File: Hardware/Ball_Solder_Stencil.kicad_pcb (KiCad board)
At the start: 4 copper layers, 99.8 x 102.2 mm, 88 parts, among them Q1 SI2333DS, U1 STM32WB35, U2 L3GD20, U2 LD1117-3.3-4Tab, U3 MCP73831-2-OT, U3 TL074, U4 LD3985M28R_SOT23, U4 TL072, Y1 32MHz, Y2 32.768MHz

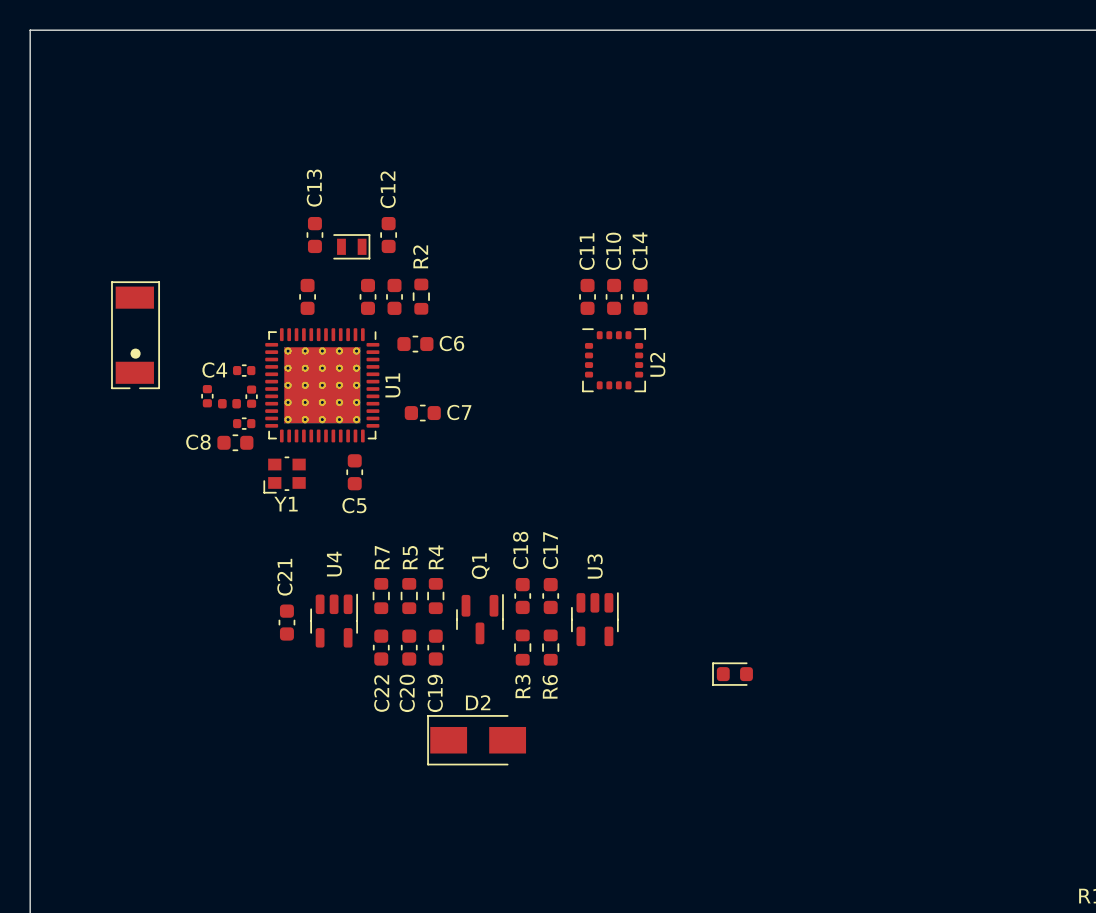
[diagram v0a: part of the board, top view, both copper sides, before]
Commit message: More PCB clean-up
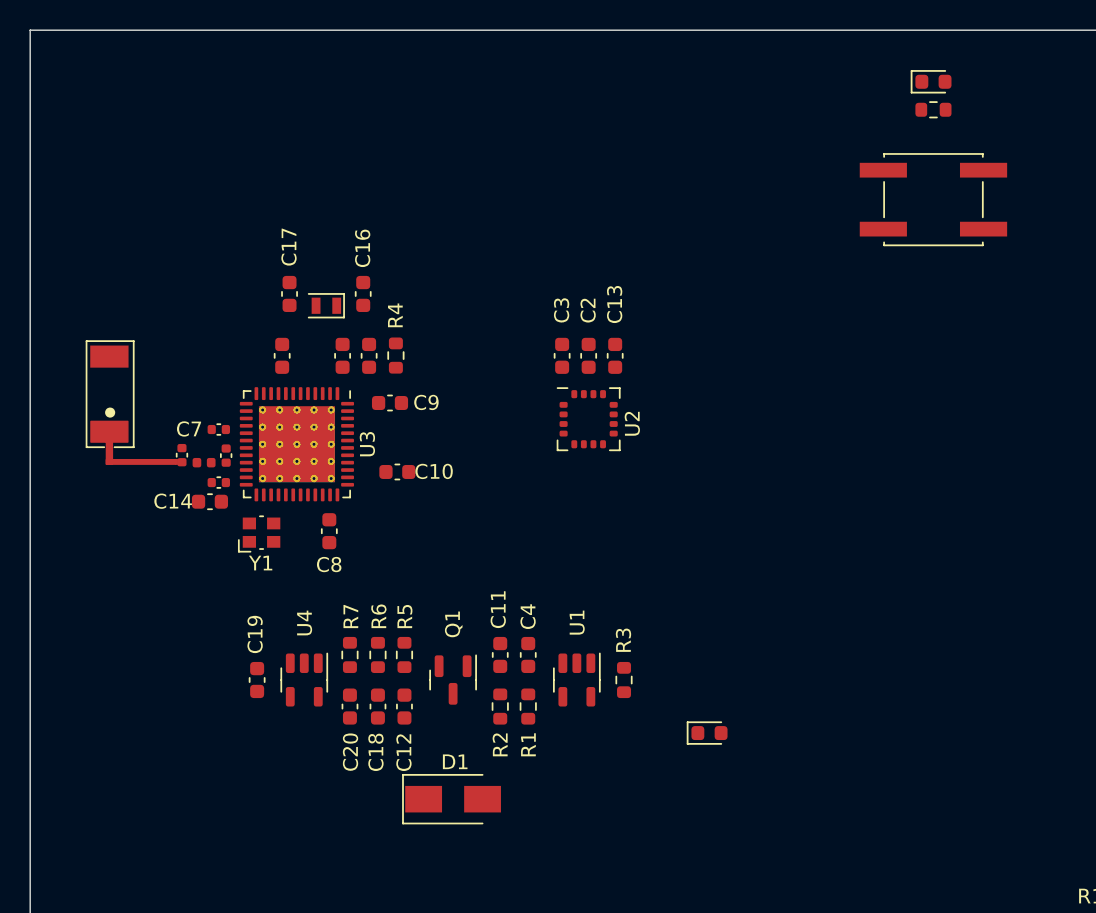
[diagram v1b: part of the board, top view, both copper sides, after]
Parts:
- added CONNECT1: SW_Push, Button_Switch_SMD:SW_SPST_EVQQ2, F.Cu at (126.3, 67.1)
- added D1: PMEG3010ER, Diode_SMD:D_SMA, F.Cu at (93.7, 107.8)
- added R1: 1k, Resistor_SMD:R_0603_1608Metric, F.Cu at (98.8, 101.5)
- added R8: 1k, Resistor_SMD:R_0603_1608Metric, F.Cu at (126.3, 61.0)
- C11: value 10uF -> 4.7uF
- C12: value 16pF -> 1uF
- C13: value 16pF -> 10nF
- C14: value 10nF -> 100nF
- C15: value 0.8pF -> 100pF
- C16: value 0.3pF -> 16pF; footprint Capacitor_SMD:C_0402_1005Metric -> Capacitor_SMD:C_0603_1608Metric
- C17: value 4.7uF -> 16pF
- C18: value 4.7uF -> 1uF
- C19: value 1uF -> 10nF
- C2: value 4.7uF -> 100nF
- C21: value 10nF -> 0.8pF; footprint Capacitor_SMD:C_0603_1608Metric -> Capacitor_SMD:C_0402_1005Metric
- C22: value 1uF -> 0.3pF; footprint Capacitor_SMD:C_0603_1608Metric -> Capacitor_SMD:C_0402_1005Metric
- C3: value 100nF -> 10uF
- C4: value 100nF -> 4.7uF; footprint Capacitor_SMD:C_0402_1005Metric -> Capacitor_SMD:C_0603_1608Metric
- C5: value 100nF -> 4.7uF
- C7: footprint Capacitor_SMD:C_0603_1608Metric -> Capacitor_SMD:C_0402_1005Metric
- C9: value 100pF -> 100nF; footprint Capacitor_SMD:C_0402_1005Metric -> Capacitor_SMD:C_0603_1608Metric
- D2: value PMEG3010ER -> LED_CHG; footprint Diode_SMD:D_SMA -> LED_SMD:LED_0603_1608Metric
- D3: value LED_CHG -> LED_CONNECT
- R3: value 1k -> 10k
- R4: value 27k -> 100k
- R5: value 13k -> 27k
- R6: value 10k -> 13k
- U1: value STM32WB35 -> MCP73831-2-OT; footprint Package_DFN_QFN:QFN-48-1EP_7x7mm_P0.5mm_EP5.15x5.15mm_ThermalVias -> Package_TO_SOT_SMD:SOT-23-5
- U3: value MCP73831-2-OT -> STM32WB35; footprint Package_TO_SOT_SMD:SOT-23-5 -> Package_DFN_QFN:QFN-48-1EP_7x7mm_P0.5mm_EP5.15x5.15mm_ThermalVias
- moved D3 42.4 mm to (126.3, 59.1)
- moved C14 32.4 mm to (77.2, 87.6), turned to 180 degrees
- moved C12 32.0 mm to (90.4, 101.5)
- moved R2 28.3 mm to (96.9, 101.5)
- moved C4 27.3 mm to (98.8, 98.0), turned to 90 degrees
- moved C17 27.1 mm to (82.6, 73.5), turned to -90 degrees
- moved U1 26.4 mm to (102.1, 99.7)
- moved C11 25.0 mm to (96.9, 98.0), turned to -90 degrees
- moved U3 23.5 mm to (83.1, 83.7)
- moved C13 22.0 mm to (104.7, 77.7), turned to 90 degrees
- moved C10 18.9 mm to (89.9, 85.6), turned to 0 degrees
- moved C22 18.8 mm to (75.3, 84.4)
- moved R4 16.5 mm to (89.8, 77.7)
- moved D2 15.7 mm to (111.1, 103.3)
- moved C7 13.9 mm to (77.8, 82.7), turned to 180 degrees
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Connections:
- AE1 pad 1: (no net) -> Net-(AE1-Pad1)
- AE1 pad 2: (no net) -> unconnected-(AE1-Pad2)
- C12 pad 1: GND -> VCC
- C12 pad 2: (no net) -> GND
- C13 pad 1: GND -> (no net)
- C13 pad 2: (no net) -> GND
- C15 pad 1: /RF_Output -> (no net)
- C16 pad 1: Net-(AE1-Pad1) -> GND
- C16 pad 2: GND -> (no net)
- C17 pad 1: (no net) -> GND
- C17 pad 2: GND -> Net-(C17-Pad2)
- C18 pad 1: (no net) -> VCC
- C19 pad 1: VCC -> (no net)
- C20 pad 1: VCC -> (no net)
- C21 pad 1: (no net) -> /RF_Output
- C22 pad 1: (no net) -> Net-(AE1-Pad1)
- D2 pad 1: VCC -> (no net)
- D3 pad 1: (no net) -> Net-(D3-Pad1)
- D3 pad 2: (no net) -> /LED_BLUE_OUT
- R2 pad 2: /BOOT0 -> (no net)
- R3 pad 1: (no net) -> GND
- R4 pad 1: VCC -> GND
- R4 pad 2: (no net) -> /BOOT0
- R5 pad 1: (no net) -> VCC
- R6 pad 1: GND -> (no net)
- U1 pad 2: (no net) -> GND
- U1 pad 4: /BOOT0 -> (no net)
- U3 pad 2: GND -> (no net)
- U3 pad 3: (no net) -> Net-(C17-Pad2)
- U3 pad 4: (no net) -> /BOOT0
- Y1 pad 1: Net-(U1-Pad24) -> (no net)
- Y1 pad 3: Net-(U1-Pad25) -> (no net)
- Y2 pad 2: (no net) -> Net-(C17-Pad2)

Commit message: Preparation of Gerbers for manufacturing
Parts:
- removed the AE1 at (74.9, 84.9)
- removed the AE1 at (128.4, 147.8)
- removed the C1 at (141.3, 140.6)
- removed the C1 at (82.1, 77.7)
- removed the C10 at (89.9, 85.6)
- removed the C10 at (155.2, 90.7)
- removed the C11 at (96.9, 98.0)
- removed the C11 at (155.2, 60.5)
- removed the C12 at (131.8, 147.4)
- removed the C12 at (90.4, 101.5)
- removed the C13 at (104.7, 77.7)
- removed the C13 at (128.8, 147.3)
- removed the C14 at (157.3, 109.8)
- removed the C14 at (77.2, 87.6)
- removed the C15 at (77.8, 86.3)
- removed the C15 at (140.4, 128.0)
- removed the C16 at (87.6, 73.5)
- removed the C16 at (152.6, 128.0)
- removed the C17 at (82.6, 73.5)
- removed the C17 at (140.4, 129.7)
- removed the C18 at (88.6, 101.5)
- removed the C18 at (152.6, 126.3)
- removed the C19 at (152.6, 117.8)
- removed the C19 at (80.4, 99.7)
- removed the C2 at (102.9, 77.7)
- removed the C2 at (139.5, 140.6)
- removed the C20 at (86.7, 101.5)
- removed the C20 at (152.6, 124.6)
- removed the C21 at (78.3, 84.5)
- removed the C21 at (140.4, 119.5)
- removed the C22 at (140.4, 124.6)
- removed the C22 at (75.3, 84.4)
- removed the C3 at (101.1, 77.7)
- removed the C3 at (131.3, 145.6)
- removed the C4 at (138.8, 152.5)
- removed the C4 at (98.8, 98.0)
- removed the C5 at (142.9, 143.8)
- removed the C5 at (88.0, 77.7)
- removed the C6 at (142.9, 147.8)
- removed the C6 at (86.2, 77.7)
- removed the C7 at (135.9, 140.6)
- removed the C7 at (77.8, 82.7)
- removed the C8 at (130.7, 150.5)
- removed the C8 at (85.3, 89.6)
- removed the C9 at (89.4, 80.9)
- removed the C9 at (131.3, 149.2)
- removed the D1 at (159.7, 90.7)
- removed the D1 at (93.7, 107.8)
- removed the D2 at (111.1, 103.3)
- removed the D2 at (159.7, 60.5)
- removed the D3 at (126.3, 59.1)
- removed the L1 at (76.8, 85.0)
- removed the L1 at (130.3, 147.8)
- removed the Q1 at (93.7, 99.7)
- removed the R1 at (98.8, 101.5)
- removed the R1 at (137.7, 140.6)
- removed the R10 at (140.4, 121.2)
- removed the R11 at (140.4, 122.9)
- removed the R12 at (140.4, 116.1)
- removed the R13 at (140.4, 117.8)
- removed the R14 at (152.6, 116.1)
- removed the R15 at (140.4, 126.3)
- removed the R16 at (140.4, 114.4)
- removed the R17 at (130.8, 143.2)
- removed the R2 at (140.4, 131.4)
- removed the R2 at (96.9, 101.5)
- removed the R3 at (105.3, 99.7)
- removed the R3 at (152.6, 129.7)
- removed the R4 at (152.6, 133.1)
- removed the R4 at (89.8, 77.7)
- removed the R5 at (152.6, 131.4)
- removed the R5 at (90.4, 98.0)
- removed the R6 at (88.6, 98.0)
- removed the R6 at (140.4, 133.1)
- removed the R7 at (86.7, 98.0)
- removed the R7 at (152.6, 122.9)
- removed the R8 at (126.3, 61.0)
- removed the R8 at (152.6, 119.5)
- removed the R9 at (152.6, 121.2)
- removed the U1 at (102.1, 99.7)
- removed the U1 at (136.6, 146.6)
- removed the U2 at (102.9, 82.0)
- removed the U2 at (157.3, 100.2)
- removed the U3 at (83.1, 83.7)
- removed the U3 at (146.5, 128.5)
- removed the U4 at (83.6, 99.7)
- removed the U4 at (146.5, 117.0)
- removed the Y1 at (134.2, 152.6)
- removed the Y1 at (80.7, 89.7)
- added AE1: Antenna_Shield, Custom_Footprints:NN01_102, F.Cu at (125.9, 132.9)
- added AE1: Antenna_Shield, Custom_Footprints:NN01_102, F.Cu at (214.0, 94.9)
- added C1: 4.7uF, Capacitor_SMD:C_0603_1608Metric, F.Cu at (138.7, 125.8)
- added C1: 4.7uF, Capacitor_SMD:C_0603_1608Metric, F.Cu at (58.4, 96.8)
- added C1: 100nF, Capacitor_SMD:C_0603_1608Metric, F.Cu at (221.2, 87.7)
- added C10: 22uF, Capacitor_SMD:CP_Elec_4x5.4, F.Cu at (148.9, 75.8)
- added C10: 100nF, Capacitor_SMD:C_0603_1608Metric, F.Cu at (229.0, 95.6)
- added C10: 18pF, Capacitor_SMD:C_0603_1608Metric, F.Cu at (52.5, 99.7)
- added C11: 18pF, Capacitor_SMD:C_0603_1608Metric, F.Cu at (52.5, 103.5)
- added C11: 4.7uF, Capacitor_SMD:C_0603_1608Metric, F.Cu at (236.0, 108.0)
- added C11: 22uF, Capacitor_SMD:CP_Elec_4x5.4, F.Cu at (148.9, 45.6)
- added C12: 0.8pF, Capacitor_SMD:C_0402_1005Metric, F.Cu at (129.2, 132.5)
- added C12: 2.2nF, Capacitor_SMD:C_0603_1608Metric, F.Cu at (68.4, 128.1)
- added C12: 1uF, Capacitor_SMD:C_0603_1608Metric, F.Cu at (229.5, 111.5)
- added C13: 0.3pF, Capacitor_SMD:C_0402_1005Metric, F.Cu at (126.2, 132.5)
- added C13: 10nF, Capacitor_SMD:C_0603_1608Metric, F.Cu at (243.8, 87.7)
- added C13: 1.5nF, Capacitor_SMD:C_0603_1608Metric, F.Cu at (68.4, 116.1)
- added C14: 47uF, Capacitor_SMD:CP_Elec_5x5.8, F.Cu at (151.0, 95.0)
- added C14: 2.2nF, Capacitor_SMD:C_0603_1608Metric, F.Cu at (55.6, 116.1)
- added C14: 100nF, Capacitor_SMD:C_0603_1608Metric, F.Cu at (216.3, 97.6)
- added C15: 100nF, Capacitor_SMD:C_0603_1608Metric, F.Cu at (134.1, 113.2)
- added C15: 100pF, Capacitor_SMD:C_0402_1005Metric, F.Cu at (216.9, 96.3)
- added C15: 1.5nF, Capacitor_SMD:C_0603_1608Metric, F.Cu at (55.6, 128.1)
- added C16: 16pF, Capacitor_SMD:C_0603_1608Metric, F.Cu at (226.7, 83.5)
- added C16: 18pF, Capacitor_SMD:C_0603_1608Metric, F.Cu at (55.6, 84.0)
- added C16: 100nF, Capacitor_SMD:C_0603_1608Metric, F.Cu at (146.3, 113.2)
- added C17: 22nF, Capacitor_SMD:C_0603_1608Metric, F.Cu at (134.1, 114.8)
- added C17: 16pF, Capacitor_SMD:C_0603_1608Metric, F.Cu at (221.7, 83.5)
- added C17: 10uF, Capacitor_SMD:C_0603_1608Metric, F.Cu at (55.6, 89.7)
- added C18: 1uF, Capacitor_SMD:C_0603_1608Metric, F.Cu at (227.7, 111.5)
- added C18: 33nF, Capacitor_SMD:C_0603_1608Metric, F.Cu at (146.3, 111.5)
- added C18: 18pF, Capacitor_SMD:C_0603_1608Metric, F.Cu at (68.4, 84.0)
- added C19: 10uF, Capacitor_SMD:C_0603_1608Metric, F.Cu at (68.4, 89.7)
- added C19: 22nF, Capacitor_SMD:C_0603_1608Metric, F.Cu at (146.3, 103.0)
- added C19: 10nF, Capacitor_SMD:C_0603_1608Metric, F.Cu at (219.5, 109.7)
- added C2: 100nF, Capacitor_SMD:C_0603_1608Metric, F.Cu at (136.9, 125.8)
- added C2: 100nF, Capacitor_SMD:C_0603_1608Metric, F.Cu at (62.6, 111.9)
- added C2: 100nF, Capacitor_SMD:C_0603_1608Metric, F.Cu at (242.0, 87.7)
- added C20: 1uF, Capacitor_SMD:C_0603_1608Metric, F.Cu at (225.8, 111.5)
- added C20: 10uF, Capacitor_SMD:C_0805_2012Metric, F.Cu at (51.7, 52.4)
- added C20: 33nF, Capacitor_SMD:C_0603_1608Metric, F.Cu at (146.3, 109.8)
- added C21: 22uF, Capacitor_SMD:CP_Elec_4x5.3, F.Cu at (80.8, 72.8)
- added C21: 22nF, Capacitor_SMD:C_0603_1608Metric, F.Cu at (134.1, 104.7)
- added C21: 0.8pF, Capacitor_SMD:C_0402_1005Metric, F.Cu at (217.4, 94.5)
- added C22: 33nF, Capacitor_SMD:C_0603_1608Metric, F.Cu at (134.1, 109.8)
- added C22: 0.3pF, Capacitor_SMD:C_0402_1005Metric, F.Cu at (214.4, 94.4)
- added C22: 47uF, Capacitor_SMD:CP_Elec_5x5.4, F.Cu at (59.9, 52.4)
- added C23: 100nF, Capacitor_SMD:C_0603_1608Metric, F.Cu at (37.6, 74.0)
- added C24: 22uF, Capacitor_SMD:CP_Elec_4x5.3, F.Cu at (42.9, 72.8)
- added C3: 100nF, Capacitor_SMD:C_0603_1608Metric, F.Cu at (69.3, 111.9)
- added C3: 100nF, Capacitor_SMD:C_0402_1005Metric, F.Cu at (128.7, 130.8)
- added C3: 10uF, Capacitor_SMD:C_0603_1608Metric, F.Cu at (240.2, 87.7)
- added C4: 4.7uF, Capacitor_SMD:C_0603_1608Metric, F.Cu at (237.9, 108.0)
- added C4: 100nF, Capacitor_SMD:C_0603_1608Metric, F.Cu at (136.2, 137.7)
- added C4: 100nF, Capacitor_SMD:C_0603_1608Metric, F.Cu at (74.4, 98.8)
- added C5: 100nF, Capacitor_SMD:C_0603_1608Metric, F.Cu at (140.4, 128.9)
- added C5: 100nF, Capacitor_SMD:C_0603_1608Metric, F.Cu at (61.6, 94.3)
- added C5: 4.7uF, Capacitor_SMD:C_0603_1608Metric, F.Cu at (227.1, 87.7)
- added C6: 100nF, Capacitor_SMD:C_0603_1608Metric, F.Cu at (225.3, 87.7)
- added C6: 100nF, Capacitor_SMD:C_0603_1608Metric, F.Cu at (140.3, 132.9)
- added C6: 1uF, Capacitor_SMD:C_0603_1608Metric, F.Cu at (56.4, 108.3)
- added C7: 100nF, Capacitor_SMD:C_0603_1608Metric, F.Cu at (133.3, 125.8)
- added C7: 100nF, Capacitor_SMD:C_0402_1005Metric, F.Cu at (216.9, 92.7)
- added C7: 100nF, Capacitor_SMD:C_0603_1608Metric, F.Cu at (56.4, 106.6)
- added C8: 100nF, Capacitor_SMD:C_0603_1608Metric, F.Cu at (128.1, 135.7)
- added C8: 100nF, Capacitor_SMD:C_0603_1608Metric, F.Cu at (224.4, 99.6)
- added C8: 2.2uF, Capacitor_SMD:C_0603_1608Metric, F.Cu at (67.6, 111.9)
- added C9: 100pF, Capacitor_SMD:C_0402_1005Metric, F.Cu at (128.7, 134.3)
- added C9: 100nF, Capacitor_SMD:C_0603_1608Metric, F.Cu at (228.5, 90.9)
- added C9: 2.2uF, Capacitor_SMD:C_0603_1608Metric, F.Cu at (74.4, 100.5)
- added D1: PMEG3010ER, Diode_SMD:D_SMA, F.Cu at (232.8, 117.8)
- added D1: 1N5819, Diode_SMD:D_SOD-123, F.Cu at (153.4, 75.8)
- added D2: LED_CHG, LED_SMD:LED_0603_1608Metric, F.Cu at (250.2, 113.3)
- added D2: 1N5819, Diode_SMD:D_SOD-123, F.Cu at (153.4, 45.6)
- added D2: 1N5819, Diode_SMD:D_SOD-123, F.Cu at (76.2, 72.8)
- added D3: LED_CONNECT, LED_SMD:LED_0603_1608Metric, F.Cu at (265.4, 69.1)
- added D3: 1N5819, Diode_SMD:D_SOD-123, F.Cu at (47.4, 72.8)
- added J2: USB_B_Micro, Custom_Footprints:USB_Micro-B_Amphenol, F.Cu at (265.4, 114.3)
- added J3: USB_B_Micro, Custom_Footprints:USB_Micro-B_Amphenol, F.Cu at (152.3, 135.3)
- added L1: 2.7nH, Inductor_SMD:L_0402_1005Metric, F.Cu at (215.9, 95.0)
- added L1: 2.7nH, Inductor_SMD:L_0402_1005Metric, F.Cu at (127.7, 133.0)
- added L1: L, Inductor_SMD:L_0805_2012Metric, F.Cu at (54.7, 52.4)
- added Q1: MMBT3904, Package_TO_SOT_SMD:SOT-23, F.Cu at (64.4, 133.7)
- added Q1: SI2333DS, Package_TO_SOT_SMD:SOT-23, F.Cu at (232.8, 109.7)
- added Q2: MMBT3904, Package_TO_SOT_SMD:SOT-23, F.Cu at (59.6, 133.7)
- added R1: 100k, Resistor_SMD:R_0603_1608Metric, F.Cu at (135.1, 125.8)
- added R1: 1k, Resistor_SMD:R_0603_1608Metric, F.Cu at (237.9, 111.5)
- added R1: 100k, Resistor_SMD:R_0603_1608Metric, F.Cu at (63.7, 94.3)
- added R10: 68k, Resistor_SMD:R_0603_1608Metric, F.Cu at (55.6, 120.1)
- added R10: 20k, Resistor_SMD:R_0603_1608Metric, F.Cu at (134.1, 106.3)
- added R11: 20k, Resistor_SMD:R_0603_1608Metric, F.Cu at (134.1, 108.0)
- added R11: 47k, Resistor_SMD:R_0603_1608Metric, F.Cu at (55.6, 118.1)
- added R12: 5k1, Resistor_SMD:R_0603_1608Metric, F.Cu at (134.1, 101.2)
- added R12: 100k, Resistor_SMD:R_0603_1608Metric, F.Cu at (55.6, 122.1)
- added R13: 68k, Resistor_SMD:R_0603_1608Metric, F.Cu at (55.6, 124.1)
- added R13: 10k, Resistor_SMD:R_0603_1608Metric, F.Cu at (134.1, 103.0)
- added R14: 47k, Resistor_SMD:R_0603_1608Metric, F.Cu at (55.6, 126.1)
- added R14: 1k, Resistor_SMD:R_0603_1608Metric, F.Cu at (146.3, 101.2)
- added R15: 47k, Resistor_SMD:R_0603_1608Metric, F.Cu at (68.4, 78.3)
- added R15: 1k, Resistor_SMD:R_0603_1608Metric, F.Cu at (134.1, 111.5)
- added R16: 1k, Resistor_SMD:R_0603_1608Metric, F.Cu at (134.1, 99.5)
- added R16: 100k, Resistor_SMD:R_0603_1608Metric, F.Cu at (55.6, 130.1)
- added R17: 1k, Resistor_SMD:R_0603_1608Metric, F.Cu at (128.3, 128.4)
- added R17: 68k, Resistor_SMD:R_0603_1608Metric, F.Cu at (55.6, 82.1)
- added R18: 6.8k, Resistor_SMD:R_0603_1608Metric, F.Cu at (55.6, 85.9)
- added R19: 1k, Resistor_SMD:R_0603_1608Metric, F.Cu at (55.6, 80.2)
- added R2: 1k, Resistor_SMD:R_0603_1608Metric, F.Cu at (66.9, 59.0)
- added R2: 20k, Resistor_SMD:R_0603_1608Metric, F.Cu at (134.1, 116.5)
- added R2: 100k, Resistor_SMD:R_0603_1608Metric, F.Cu at (236.0, 111.5)
- added R20: 47k, Resistor_SMD:R_0603_1608Metric, F.Cu at (55.6, 87.8)
- added R21: 68k, Resistor_SMD:R_0603_1608Metric, F.Cu at (68.4, 82.1)
- added R22: 6.8k, Resistor_SMD:R_0603_1608Metric, F.Cu at (68.4, 85.9)
- added R23: 1k, Resistor_SMD:R_0603_1608Metric, F.Cu at (68.4, 80.2)
- added R24: 47k, Resistor_SMD:R_0603_1608Metric, F.Cu at (68.4, 87.8)
- added R25: 4k7, Resistor_SMD:R_0603_1608Metric, F.Cu at (68.4, 134.2)
- added R26: 4k7, Resistor_SMD:R_0603_1608Metric, F.Cu at (55.6, 132.1)
- added R27: 4k7, Resistor_SMD:R_0603_1608Metric, F.Cu at (68.4, 132.1)
- added R28: 2.2k, Resistor_SMD:R_0603_1608Metric, F.Cu at (37.6, 76.0)
- added R3: 10k, Resistor_SMD:R_0603_1608Metric, F.Cu at (244.4, 109.7)
- added R3: 1k, Resistor_SMD:R_0603_1608Metric, F.Cu at (55.6, 78.3)
- added R3: 20k, Resistor_SMD:R_0603_1608Metric, F.Cu at (146.3, 114.8)
- added R4: 100k, Resistor_SMD:R_0603_1608Metric, F.Cu at (228.9, 87.7)
- added R4: 5k1, Resistor_SMD:R_0603_1608Metric, F.Cu at (146.3, 118.2)
- added R4: 91k, Resistor_SMD:R_0603_1608Metric, F.Cu at (68.4, 124.1)
- added R5: 27k, Resistor_SMD:R_0603_1608Metric, F.Cu at (229.5, 108.0)
- added R5: 56k, Resistor_SMD:R_0603_1608Metric, F.Cu at (68.4, 126.1)
- added R5: 10k, Resistor_SMD:R_0603_1608Metric, F.Cu at (146.3, 116.5)
- added R6: 20k, Resistor_SMD:R_0603_1608Metric, F.Cu at (134.1, 118.2)
- added R6: 13k, Resistor_SMD:R_0603_1608Metric, F.Cu at (227.7, 108.0)
- added R6: 100k, Resistor_SMD:R_0603_1608Metric, F.Cu at (68.4, 130.1)
- added R7: 20k, Resistor_SMD:R_0603_1608Metric, F.Cu at (146.3, 108.0)
- added R7: 24k, Resistor_SMD:R_0603_1608Metric, F.Cu at (225.8, 108.0)
- added R7: 82k, Resistor_SMD:R_0603_1608Metric, F.Cu at (68.4, 120.1)
- added R8: 5k1, Resistor_SMD:R_0603_1608Metric, F.Cu at (146.3, 104.7)
- added R8: 1k, Resistor_SMD:R_0603_1608Metric, F.Cu at (265.4, 71.0)
- added R8: 47k, Resistor_SMD:R_0603_1608Metric, F.Cu at (68.4, 118.1)
- added R9: 10k, Resistor_SMD:R_0603_1608Metric, F.Cu at (146.3, 106.3)
- added R9: 100k, Resistor_SMD:R_0603_1608Metric, F.Cu at (68.4, 122.1)
- added RESET1: SW_Push, Custom_Footprints:SW_SPST_EVQQ2, F.Cu at (44.9, 95.3)
- added U1: STM32F405RGTx, Package_QFP:LQFP-64_10x10mm_P0.5mm, F.Cu at (65.4, 103.1)
- added U1: STM32WB35, Package_DFN_QFN:QFN-48-1EP_7x7mm_P0.5mm_EP5.15x5.15mm_ThermalVias, F.Cu at (134.0, 131.8)
- added U1: MCP73831-2-OT, Package_TO_SOT_SMD:SOT-23-5, F.Cu at (241.2, 109.7)
- added U2: LD1117-3.3-4Tab, Package_TO_SOT_SMD:SOT-223-3_TabPin2, F.Cu at (151.0, 85.4)
- added U2: TL072, Package_SO:SOIC-8_3.9x4.9mm_P1.27mm, F.Cu at (62.0, 85.0)
- added U2: L3GD20, Package_LGA:LGA-16_4x4mm_P0.65mm_LayoutBorder4x4y, F.Cu at (242.0, 92.0)
- added U3: TL074, Package_SO:SOIC-14_3.9x8.7mm_P1.27mm, F.Cu at (140.2, 113.7)
- added U3: STM32WB35, Package_DFN_QFN:QFN-48-1EP_7x7mm_P0.5mm_EP5.15x5.15mm_ThermalVias, F.Cu at (222.2, 93.7)
- added U3: MCP6004, Package_SO:SOIC-14_3.9x8.7mm_P1.27mm, F.Cu at (62.0, 123.1)
- added U4: LD3985M28R_SOT23, Package_TO_SOT_SMD:SOT-23-5, F.Cu at (222.7, 109.7)
- added U4: LM1117-3.3, Package_TO_SOT_SMD:SOT-223-3_TabPin2, F.Cu at (68.7, 52.2)
- added U4: TL072, Package_SO:SOIC-8_3.9x4.9mm_P1.27mm, F.Cu at (140.2, 102.2)
- added U7: LM4040DBZ-5, Package_TO_SOT_SMD:SOT-23, F.Cu at (37.6, 70.8)
- added Y1: 32MHz, Crystal:Crystal_SMD_Abracon_ABM10-4Pin_2.5x2.0mm, F.Cu at (219.8, 99.7)
- added Y1: 12MHz, Crystal:Crystal_SMD_0603-2Pin_6.0x3.5mm, F.Cu at (55.6, 101.6)
- added Y1: 32MHz, Crystal:Crystal_SMD_Abracon_ABM10-4Pin_2.5x2.0mm, F.Cu at (131.6, 137.8)
- moved Y2 139.5 mm to (224.2, 84.3)
- moved CONNECT1 139.5 mm to (265.4, 77.1)
- moved L2 15.1 mm to (134.2, 122.8)
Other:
- board size 99.8 x 102.2 mm -> 250 x 120 mm
